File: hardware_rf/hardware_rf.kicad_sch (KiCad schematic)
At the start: 63 parts, among them IC1 CC1125RHBR, IC2 BALF-SPI2-02D3, IC3 4259-63, IC4 4259-63, J1 Conn_Coaxial, J2 Conn_01x03_Socket, SW1 SW_Push, U1 RP2350A-QFN60, U2 W25Q128JVS, U3 GSQ5111, U4 SK5129, Y1 Crystal_GND24, Y2 Crystal_GND24

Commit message: Schematic Done
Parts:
- added C34, C35, C36, C39, C40: 4.7u, symbol Device:C
- added C37, C38, C43, C44: 100nF, symbol Device:C
- added C41, C42: 10u, symbol Device:C
- added C45, C46, C47: 220p, symbol Device:C
- added D1: LED, symbol Device:LED
- added D2, D3: D, symbol Device:D
- added J3: Conn_02x20_Top_Bottom, symbol Connector_Generic:Conn_02x20_Top_Bottom
- added J4: USB_C_Receptacle_USB2.0_16P, symbol Connector:USB_C_Receptacle_USB2.0_16P
- added R12: 1k, symbol Device:R
- added U5: AMS1117s-3.3, Package_TO_SOT_SMD:SOT-89-3, symbol Regulator_Linear:AMS1117-3.3
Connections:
- net CTRL is gone; now on net TRX_SW: IC3.4 (CTRL), IC4.4 (CTRL)
- net 3v3: now also R11.2, U1.26 (RUN), U3.5 (VAPC1), U3.6 (VAPC2), C37.2, C38.2, D3.1 (K), J3.2 (Pin_2)
- net CSN: no longer IC1.11 (CSN)
- net GND: now also C34.2, C35.2, C36.2, C37.1, C38.1, C39.2, C40.2, C41.2, C42.2, J3.1 (Pin_1), J3.20 (Pin_20), J4.A1 (GND), J4.A12 (GND), J4.B1 (GND), J4.B12 (GND), J4.S1 (SHIELD), R12.2, U5.1 (GND)
- net GPIO0: now also U1.7 (GPIO4)
- net GPIO2: now also U1.8 (GPIO5)
- net GPIO3: now also U1.9 (GPIO6)
- net MISO: no longer IC1.9 (SO(GPIO1))
- net MOSI: no longer IC1.7 (SI)
- net RSTN: no longer IC1.2 (RESET_N)
- net SCLK: no longer IC1.8 (SCLK)
- net USB_DM: now also J4.A7 (D-), J4.B7 (D-)
- net USB_DP: now also J4.A6 (D+), J4.B6 (D+)
- net 5v: now reaches U3.15 (VCC2)
- net 5v: now also U3.16 (VCC2), U3.4 (VCC1), C34.1, C35.1, C36.1, C39.1, C40.1, C41.1, D2.1 (K), J3.23 (Pin_23), J3.3 (Pin_3), U5.3 (VI)
- net at IC3.3 (RF2): now also C46.1; no longer U3.2 (RF_IN)
- net at IC3.1 (RF1): now also C47.1; no longer U4.3 (LNA_IN)
- net I2C0_SDA: now reaches U1.12 (GPIO8)
- net I2C0_SDA: now also J3.13 (Pin_13)
- net I2C0_SCL: now reaches U1.13 (GPIO9)
- net I2C0_SCL: now also J3.12 (Pin_12)
- net SPI1_MISO: now reaches U1.16 (GPIO12)
- net SPI1_MISO: now also J3.37 (Pin_37)
- net SPI1_DEV1: now reaches U1.17 (GPIO13)
- net SPI1_DEV1: now also J3.36 (Pin_36)
- net SPI1_SCLK: now reaches U1.18 (GPIO14)
- net SPI1_SCLK: now also J3.39 (Pin_39)
- net SPI1_MOSI: now reaches U1.19 (GPIO15)
- net SPI1_MOSI: now also J3.38 (Pin_38)
- net BEAT: now reaches U1.2 (GPIO0)
- net BEAT: now also J3.31 (Pin_31)
- net SPI1_DEV3: now reaches U1.27 (GPIO16)
- net SPI1_DEV3: now also J3.34 (Pin_34)
- net SPI1_DEV2: now reaches U1.28 (GPIO17)
- net SPI1_DEV2: now also J3.35 (Pin_35)
- net SPI0_DEV2: now reaches U1.29 (GPIO18)
- net SPI0_DEV2: now also J3.15 (Pin_15)
- net SPI0_DEV3: now reaches U1.31 (GPIO19)
- net SPI0_DEV3: now also J3.14 (Pin_14)
- net SPI0_MISO: now reaches U1.32 (GPIO20)
- net SPI0_MISO: now also IC1.9 (SO(GPIO1)), J3.17 (Pin_17)
- net SPI0_DEV1: now reaches U1.33 (GPIO21)
- net SPI0_DEV1: now also IC1.11 (CSN), J3.16 (Pin_16)
- net SPI0_SCLK: now reaches U1.34 (GPIO22)
- net SPI0_SCLK: now also IC1.8 (SCLK), J3.19 (Pin_19)
- net SPI0_MOSI: now reaches U1.35 (GPIO23)
- net SPI0_MOSI: now also IC1.7 (SI), J3.18 (Pin_18)
- net CC_RSTN: now reaches U1.36 (GPIO24)
- net CC_RSTN: now also IC1.2 (RESET_N)
- net at U1.37 (GPIO25): now also D1.2 (A)
- net I2C1_SDA: now reaches U1.4 (GPIO2)
- net I2C1_SDA: now also J3.33 (Pin_33)
- net I2C1_SCL: now reaches U1.5 (GPIO3)
- net I2C1_SCL: now also J3.32 (Pin_32)
- net at IC2.5 (ANT): now also C45.1; no longer IC3.5 (RFC)
- new net: D2.2 (A), J4.A4 (VBUS), J4.A9 (VBUS), J4.B4 (VBUS), J4.B9 (VBUS)
- new net: C47.2, U4.3 (LNA_IN)
- new net: C42.1, D3.2 (A), U5.2 (VO)
- new net: C46.2, U3.2 (RF_IN)
- new net: C45.2, IC3.5 (RFC)
- new net: D1.1 (K), R12.1
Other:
- note added: "SAT_BUS"

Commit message: assignment
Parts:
- added C48, C49: 220p, Capacitor_SMD:C_0402_1005Metric, symbol Device:C
- C1, C10, C11, C12, C13, C14, C15, C16, C17, C18, C19, C2, C20, C21, C22, C23, C24, C25, C26, C27, C28, C29, C3, C30, C31, C32, C33, C34, C35, C36, C37, C38, C39, C4, C40, C45, C46, C47, C5, C6, C7, C8, C9: footprint (none) -> Capacitor_SMD:C_0402_1005Metric
- C41, C42: footprint (none) -> Capacitor_SMD:C_0805_2012Metric
- C43: value 100nF -> 1200p; footprint (none) -> Capacitor_SMD:C_0402_1005Metric
- C44: value 100nF -> 5p; footprint (none) -> Capacitor_SMD:C_0402_1005Metric
- J2: footprint (none) -> Connector_PinHeader_2.54mm:PinHeader_1x03_P2.54mm_Vertical
- J3: footprint (none) -> Connector_PinHeader_2.54mm:PinHeader_2x20_P2.54mm_Vertical
- J4: footprint (none) -> Connector_USB:USB_C_Receptacle_XKB_U262-16XN-4BVC11
- Y1, Y2: footprint (none) -> Crystal:Crystal_SMD_3225-4Pin_3.2x2.5mm
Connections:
- net GND: now also C43.2, C44.2
- net at C44.1: now also C43.1, U3.7 (2f0)
- net at U3.10 (RF_OUT), U3.11 (RF_OUT), U3.12 (RF_OUT)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: now also C49.1; no longer IC4.3 (RF2)
- net at J1.1 (In): no longer IC4.5 (RFC)
- net at U4.5 (LNA_OUT): now also C48.1; no longer IC4.1 (RF1)
- new net: C49.2, IC4.3 (RF2)
- new net: C48.2, IC4.1 (RF1)

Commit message: Assignment of footprints
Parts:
- D1: footprint (none) -> LED_SMD:LED_0402_1005Metric
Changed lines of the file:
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@@
 			)
 		)
-		(property "Footprint" ""
+		(property "Footprint" "LED_SMD:LED_0402_1005Metric"
 			(at 275.59 144.78 0)
 			(effects

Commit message: layout
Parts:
- added H1, H2, H3, H4: MountingHole_Pad, MountingHole:MountingHole_3mm_Pad_Via, symbol Mechanical:MountingHole_Pad
- D2, D3: footprint (none) -> Diode_SMD:D_0402_1005Metric
- J1: footprint (none) -> Connector_Coaxial:SMA_Amphenol_901-143_Horizontal
- L1: footprint (none) -> easyeda2kicad:IND-SMD_L2.0-W1.6_AOTA-B201610S3R3-101-T
- R1, R11, R12, R2, R3, R4, R5, R7: footprint (none) -> Resistor_SMD:R_0402_1005Metric
- R10, R8, R9: value R -> 10k; footprint (none) -> Resistor_SMD:R_0402_1005Metric
- R6: value R -> 1k; footprint (none) -> Resistor_SMD:R_0402_1005Metric
- SW1: footprint (none) -> Button_Switch_SMD:SW_SPST_PTS810
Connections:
- net CSN is gone; now on net SPI0_DEV1: DP4.2 (Pin2)
- net MISO is gone; now on net SPI0_MISO: DP3.1 (Pin1)
- net MOSI is gone; now on net SPI0_MOSI: DP3.2 (Pin2)
- net RSTN is gone; now on net CC_RSTN: DP1.1 (Pin1)
- net SCLK is gone; now on net SPI0_SCLK: DP4.1 (Pin1)
- net GND: now also H1.1, H2.1, H3.1, H4.1

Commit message: Pcb Done
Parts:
- removed J2: Conn_01x03_Socket, Connector_PinHeader_2.54mm:PinHeader_1x03_P2.54mm_Vertical, symbol Connector:Conn_01x03_Socket
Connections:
- net at J1.1 (In): now also IC4.5 (RFC)
- net UART0_TX: now reaches U1.42 (GPIO28_ADC2)
- net UART0_TX: now also J3.24 (Pin_24)
- net UART0_RX: now reaches U1.43 (GPIO29_ADC3)
- net UART0_RX: now also J3.25 (Pin_25)
- no-connect marks 0 -> 9
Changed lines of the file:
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@@
 		(color 0 0 0 0)
 	)
+	(no_connect
+		(at 259.08 83.82)
+	)
+	(no_connect
+		(at 259.08 152.4)
+	)
+	(no_connect
+		(at 259.08 149.86)
+	)
+	(no_connect
+		(at 196.85 137.16)
+	)
+	(no_connect
+		(at 196.85 139.7)
+	)
+	(no_connect
+		(at 259.08 106.68)
+	)
+	(no_connect
+		(at 259.08 109.22)
+	)
+	(no_connect
+		(at 259.08 99.06)
+	)
+	(no_connect
+		(at 240.03 205.74)
+	)
 	(wire
 		(pts
@@
 	(wire
 		(pts
-			(xy 182.88 135.89) (xy 196.85 135.89)
-		)
-		(stroke
-			(width 0)
-			(type default)
-		)
-	)
-	(wire
-		(pts
 			(xy 180.34 76.2) (xy 196.85 76.2)
 		)
@@
 	(wire
 		(pts
-			(xy 196.85 137.16) (xy 196.85 135.89)
-		)
-		(stroke
-			(width 0)
-			(type default)
-		)
-	)
-	(wire
-		(pts
 			(xy 63.5 74.93) (xy 68.58 74.93)
 		)
@@
 	(wire
 		(pts
-			(xy 182.88 140.97) (xy 196.85 140.97)
-		)
-		(stroke
-			(width 0)
-			(type default)
-		)
-	)
-	(wire
-		(pts
 			(xy 170.18 217.17) (xy 180.34 217.17)
 		)
@@
 	(wire
 		(pts
-			(xy 196.85 140.97) (xy 196.85 139.7)
-		)
-		(stroke
-			(width 0)
-			(type default)
-		)
-	)
-	(wire
-		(pts
 			(xy 323.85 231.14) (xy 323.85 227.33)
 		)
@@
 	(wire
 		(pts
+			(xy 307.34 231.14) (xy 323.85 231.14)
+		)
+		(stroke
+			(width 0)
+			(type default)
+		)
+	)
+	(wire
+		(pts
 			(xy 181.61 40.64) (xy 191.77 40.64)
 		)
@@
 		)
 	)
+	(global_label "UART0_RX"
+		(shape input)
+		(at 328.93 146.05 0)
+		(fields_autoplaced yes)
+		(effects
+			(font
+				(size 1.27 1.27)
+			)
+			(justify left)
+		)
+		(property "Intersheetrefs" "${INTERSHEET_REFS}"
+			(at 341.2285 146.05 0)
+			(effects
+				(font
+					(size 1.27 1.27)
+				)
+				(justify left)
+				(hide yes)
+			)
+		)
+	)
 	(global_label "SPI0_DEV3"
 		(shape input)
@@
 		)
 	)
+	(global_label "UART0_TX"
+		(shape input)
+		(at 328.93 143.51 0)
+		(fields_autoplaced yes)
+		(effects
+			(font
+				(size 1.27 1.27)
+			)
+			(justify left)
+		)
+		(property "Intersheetrefs" "${INTERSHEET_REFS}"
+			(at 340.9261 143.51 0)
+			(effects
+				(font
+					(size 1.27 1.27)
+				)
+				(justify left)
+				(hide yes)
+			)
+		)
+	)
 	(global_label "CC_RSTN"
 		(shape input)
@@
 		)
 	)
+	(global_label "UART0_TX"
+		(shape input)
+		(at 259.08 154.94 0)
+		(fields_autoplaced yes)
+		(effects
+			(font
+				(size 1.27 1.27)
+			)
+			(justify left)
+		)
+		(property "Intersheetrefs" "${INTERSHEET_REFS}"
+			(at 271.0761 154.94 0)
+			(effects
+				(font
+					(size 1.27 1.27)
+				)
+				(justify left)
+				(hide yes)
+			)
+		)
+	)
 	(global_label "3v3"
 		(shape input)
@@
 	(global_label "GND"
 		(shape input)
-		(at 182.88 138.43 0)
-		(fields_autoplaced yes)
-		(effects
-			(font
-				(size 1.27 1.27)
-			)
-			(justify left)
-		)
-		(property "Intersheetrefs" "${INTERSHEET_REFS}"
-			(at 189.7357 138.43 0)
-			(effects
-				(font
-					(size 1.27 1.27)
-				)
-				(justify left)
-				(hide yes)
-			)
-		)
-	)
-	(global_label "GND"
-		(shape input)
 		(at 130.81 186.69 270)
 		(fields_autoplaced yes)
@@
 		)
 	)
+	(global_label "UART0_RX"
+		(shape input)
+		(at 259.08 157.48 0)
+		(fields_autoplaced yes)
+		(effects
+			(font
+				(size 1.27 1.27)
+			)
+			(justify left)
+		)
+		(property "Intersheetrefs" "${INTERSHEET_REFS}"
+			(at 271.3785 157.48 0)
+			(effects
+				(font
+					(size 1.27 1.27)
+				)
+				(justify left)
+				(hide yes)
+			)
+		)
+	)
 	(global_label "3v3"
 		(shape input)
@@
 					(unit 1)
 				)
-			)
-		)
-	)
-	(symbol
-		(lib_id "Connector:Conn_01x03_Socket")
-		(at 177.8 138.43 180)
-		(unit 1)
-		(exclude_from_sim no)
-		(in_bom yes)
-		(on_board yes)
-		(dnp no)
-		(fields_autoplaced yes)
-		(property "Reference" "J2"
-			(at 178.435 130.81 0)
-			(effects
-				(font
-					(size 1.27 1.27)
-				)
-			)
-		)
-		(property "Value" "Conn_01x03_Socket"
-			(at 178.435 133.35 0)
-			(effects
-				(font
-					(size 1.27 1.27)
-				)
-			)
-		)
-		(property "Footprint" "Connector_PinHeader_2.54mm:PinHeader_1x03_P2.54mm_Vertical"
-			(at 177.8 138.43 0)
-			(effects
-				(font
-					(size 1.27 1.27)
-				)
-				(hide yes)
-			)
-		)
-		(property "Datasheet" "~"
-			(at 177.8 138.43 0)
-			(effects
-				(font
-					(size 1.27 1.27)
-				)
-				(hide yes)
-			)
-		)
-		(property "Description" "Generic connector, single row, 01x03, script generated"
-			(at 177.8 138.43 0)
-			(effects
-				(font
-					(size 1.27 1.27)
-				)
-				(hide yes)
-			)
-		)
-		(pin "3"
-		)
-		(pin "2"
-		)
-		(pin "1"
-		)
-		(instances
-			(project ""
-				(path "/76e9da14-bca7-4795-80b8-b5efcf73ac31"
-					(reference "J2")
-					(unit 1)
-				)

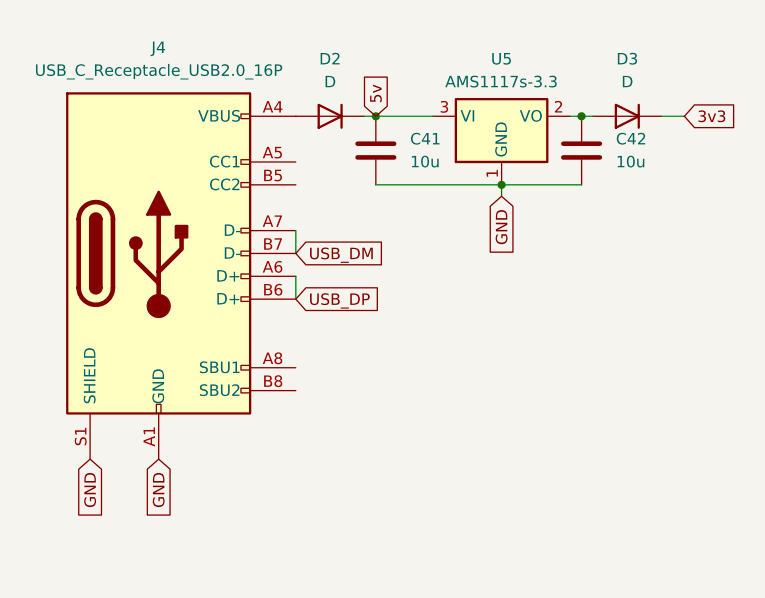
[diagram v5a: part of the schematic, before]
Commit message: CC lines on USB fixed
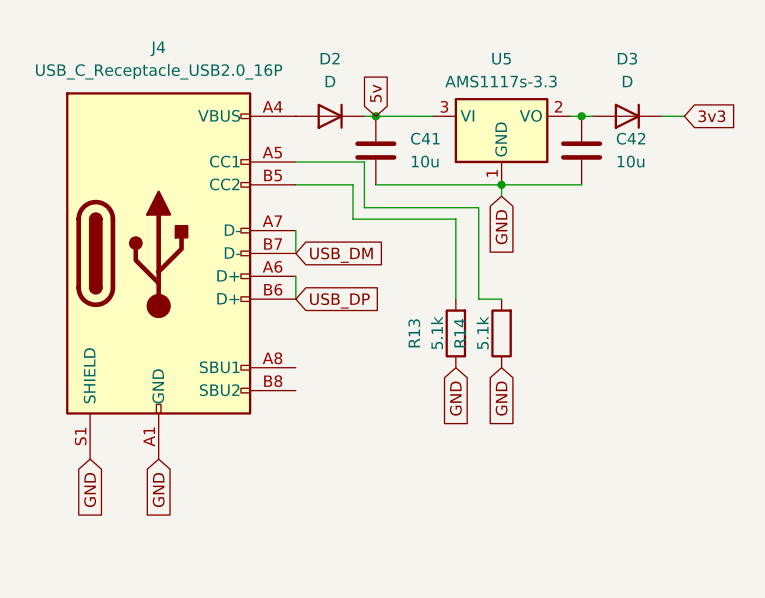
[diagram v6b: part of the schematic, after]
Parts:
- added R13, R14: 5.1k, Resistor_SMD:R_0402_1005Metric, symbol Device:R
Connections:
- net GND: now also R13.1, R14.1
- net at J4.A5 (CC1): now also R14.2
- net at J4.B5 (CC2): now also R13.2

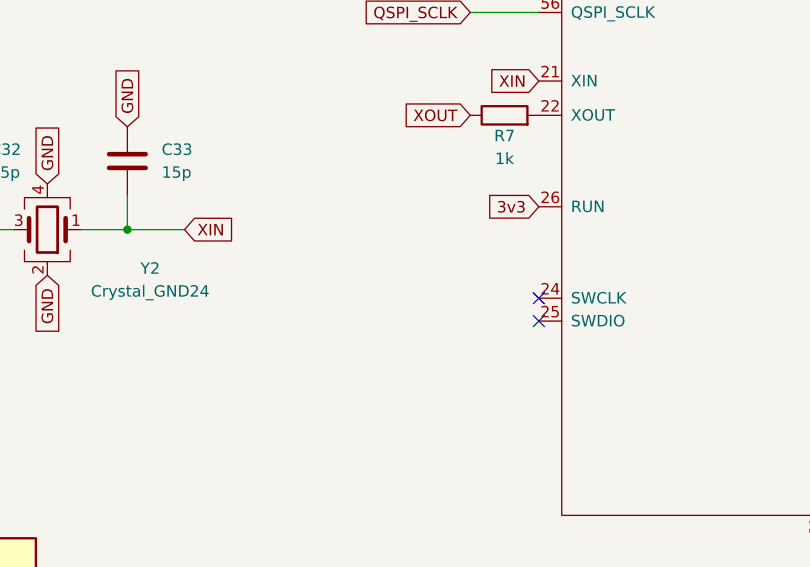
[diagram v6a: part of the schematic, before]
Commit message: Added SWD to PCB
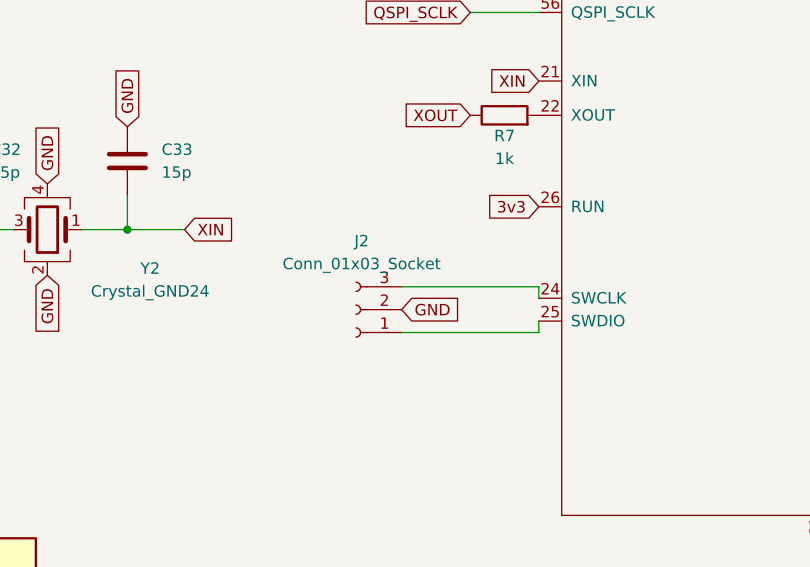
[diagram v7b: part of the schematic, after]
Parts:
- added J2: Conn_01x03_Socket, Connector_PinHeader_2.54mm:PinHeader_1x03_P2.54mm_Vertical, symbol Connector:Conn_01x03_Socket
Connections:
- net GND: now also J2.2 (Pin_2)
- net at U1.24 (SWCLK): now also J2.3 (Pin_3)
- net at U1.25 (SWDIO): now also J2.1 (Pin_1)
- no-connect marks 9 -> 7
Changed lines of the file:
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@@
 	)
 	(no_connect
-		(at 196.85 137.16)
-	)
-	(no_connect
-		(at 196.85 139.7)
-	)
-	(no_connect
 		(at 259.08 106.68)
 	)
@@
 	(wire
 		(pts
+			(xy 196.85 140.97) (xy 196.85 139.7)
+		)
+		(stroke
+			(width 0)
+			(type default)
+		)
+	)
+	(wire
+		(pts
 			(xy 60.96 156.21) (xy 62.23 156.21)
 		)
@@
 	(wire
 		(pts
+			(xy 196.85 135.89) (xy 196.85 137.16)
+		)
+		(stroke
+			(width 0)
+			(type default)
+		)
+	)
+	(wire
+		(pts
 			(xy 60.96 83.82) (xy 60.96 73.66)
 		)
@@
 	(wire
 		(pts
+			(xy 181.61 135.89) (xy 196.85 135.89)
+		)
+		(stroke
+			(width 0)
+			(type default)
+		)
+	)
+	(wire
+		(pts
 			(xy 236.22 62.23) (xy 240.03 62.23)
 		)
@@
 	(wire
 		(pts
+			(xy 181.61 140.97) (xy 196.85 140.97)
+		)
+		(stroke
+			(width 0)
+			(type default)
+		)
+	)
+	(wire
+		(pts
 			(xy 154.94 83.82) (xy 154.94 85.09)
 		)
@@
 	(global_label "GND"
 		(shape input)
+		(at 181.61 138.43 0)
+		(fields_autoplaced yes)
+		(effects
+			(font
+				(size 1.27 1.27)
+			)
+			(justify left)
+		)
+		(property "Intersheetrefs" "${INTERSHEET_REFS}"
+			(at 188.4657 138.43 0)
+			(effects
+				(font
+					(size 1.27 1.27)
+				)
+				(justify left)
+				(hide yes)
+			)
+		)
+	)
+	(global_label "GND"
+		(shape input)
 		(at 54.61 167.64 270)
 		(fields_autoplaced yes)
@@
 					(unit 1)
 				)
+			)
+		)
+	)
+	(symbol
+		(lib_id "Connector:Conn_01x03_Socket")
+		(at 176.53 138.43 180)
+		(unit 1)
+		(exclude_from_sim no)
+		(in_bom yes)
+		(on_board yes)
+		(dnp no)
+		(fields_autoplaced yes)
+		(property "Reference" "J2"
+			(at 177.165 130.81 0)
+			(effects
+				(font
+					(size 1.27 1.27)
+				)
+			)
+		)
+		(property "Value" "Conn_01x03_Socket"
+			(at 177.165 133.35 0)
+			(effects
+				(font
+					(size 1.27 1.27)
+				)
+			)
+		)
+		(property "Footprint" "Connector_PinHeader_2.54mm:PinHeader_1x03_P2.54mm_Vertical"
+			(at 176.53 138.43 0)
+			(effects
+				(font
+					(size 1.27 1.27)
+				)
+				(hide yes)
+			)
+		)
+		(property "Datasheet" "~"
+			(at 176.53 138.43 0)
+			(effects
+				(font
+					(size 1.27 1.27)
+				)
+				(hide yes)
+			)
+		)
+		(property "Description" "Generic connector, single row, 01x03, script generated"
+			(at 176.53 138.43 0)
+			(effects
+				(font
+					(size 1.27 1.27)
+				)
+				(hide yes)
+			)
+		)
+		(pin "2"
+		)
+		(pin "1"
+		)
+		(pin "3"
+		)
+		(instances
+			(project ""
+				(path "/76e9da14-bca7-4795-80b8-b5efcf73ac31"
+					(reference "J2")
+					(unit 1)
+				)
